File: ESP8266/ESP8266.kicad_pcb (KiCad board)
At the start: 2 copper layers, 50.8 x 25.4 mm, 52 parts, among them J1 TYPE-C, J2 Micro_SD_Card_Det_Hirose_DM3AT, J3 SirBlue, J4 Conn_01x11, J6 Conn_01x11, Q1 BSS138DW, Q2 MMBT2222A, U1 CP2104, U2 AZ1117-3.3, U3 ESP-12F

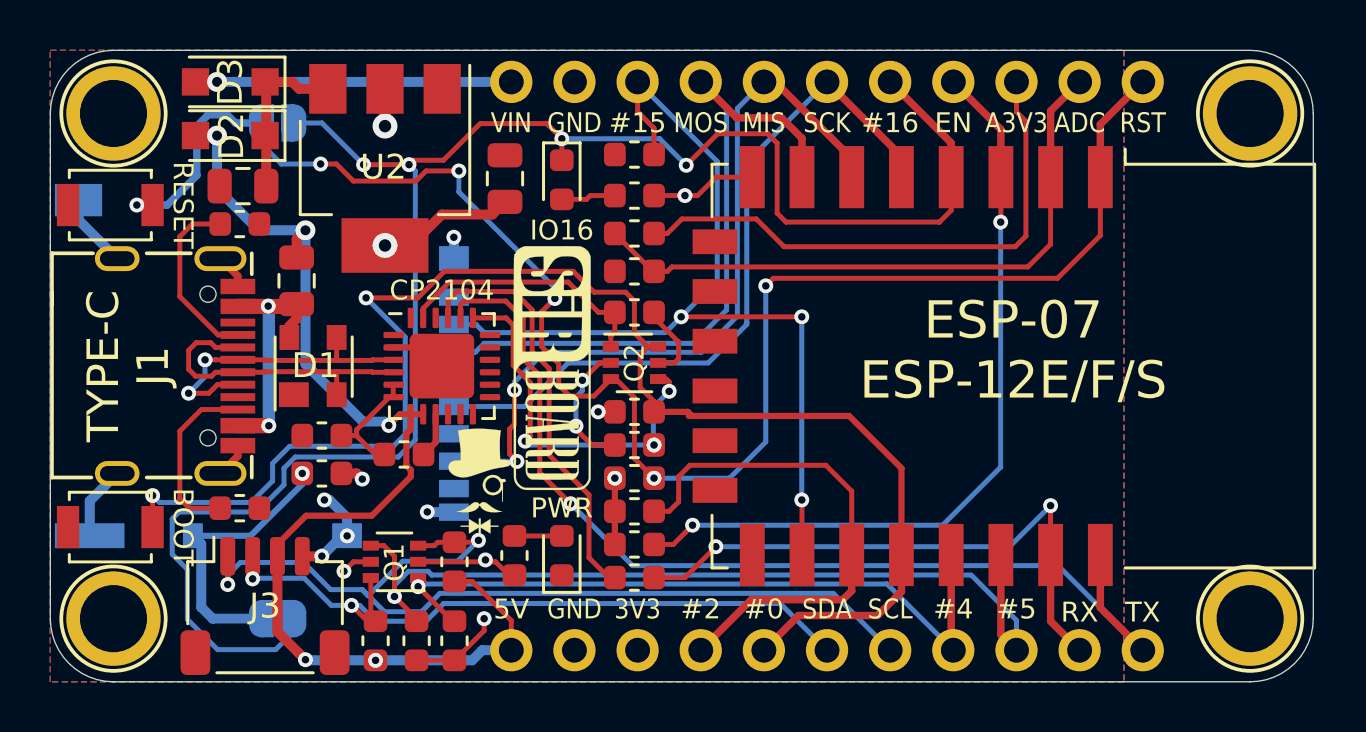
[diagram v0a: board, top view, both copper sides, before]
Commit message: ESP8266 V1.3
LED Deletes Added
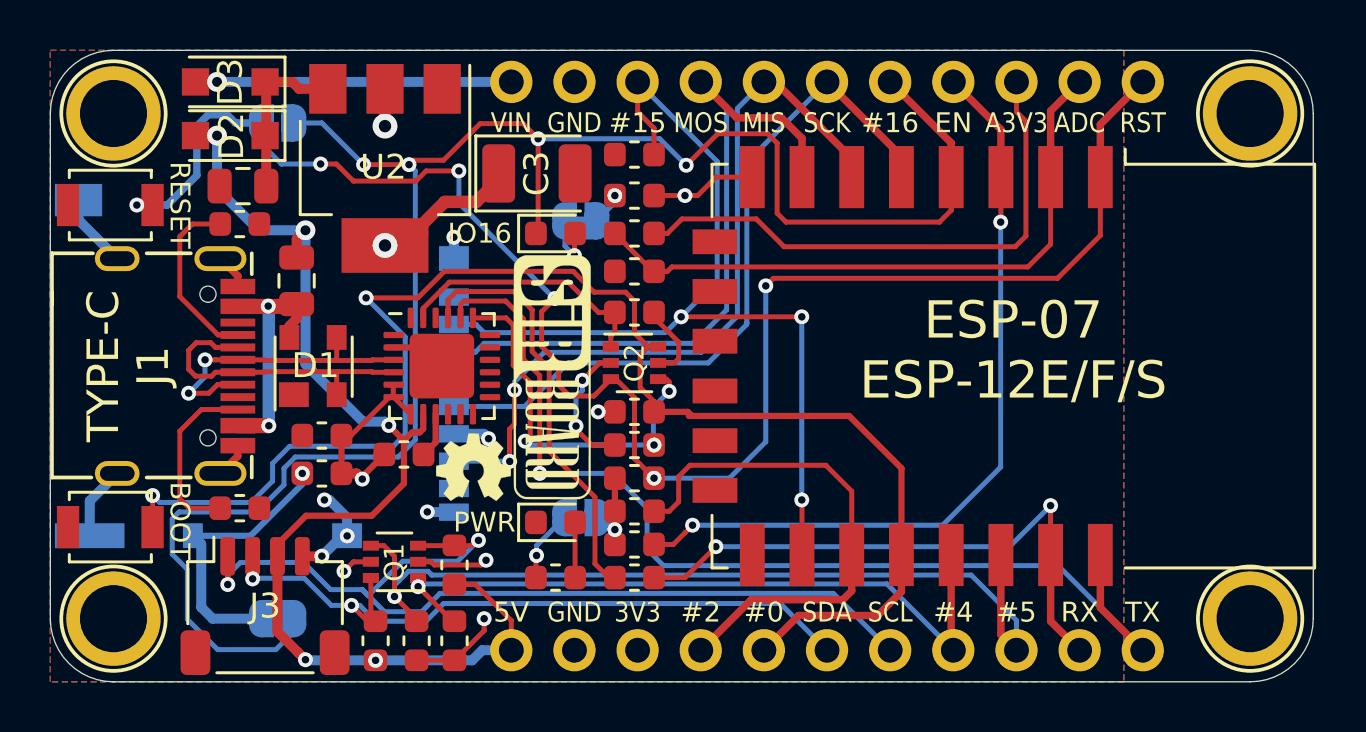
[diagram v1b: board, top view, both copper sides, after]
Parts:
- removed the G*** at (59.2, 44.0)
- added G***: LOGO, logo:OSHW44x31, F.Cu at (58.9, 43.4)
- added IO16: LED_DELETE2, SirBoardLibrary:SolderJumper-2_P1.3mm_Bridged_RoundedPad1.0x1.5mm, B.Cu at (63.2, 33.5)
- added PWR: LED_DELETE1, SirBoardLibrary:SolderJumper-2_P1.3mm_Bridged_RoundedPad1.0x1.5mm, B.Cu at (63.2, 45.5)
- C3: value 10uF -> 100uF; footprint Capacitor_SMD:C_0805_2012Metric -> Capacitor_Tantalum_SMD:CP_EIA-3528-21_Kemet-B
- HOIROSE DM3AT: renamed from J2
- moved IO16 2.17 mm to (62.2, 34.0), turned to 0 degrees
- moved R16 1.88 mm to (62.2, 47.9), turned to 0 degrees
- moved G*** 1.40 mm to (69.3, 39.4)
- moved PWR 1.36 mm to (62.2, 45.7), turned to 0 degrees
- moved C3 1.30 mm to (61.5, 31.6), turned to 0 degrees
- moved G*** 0.63 mm to (76.8, 39.4)
- moved G*** 0.37 mm to (62.1, 39.8)
- moved R7 0.13 mm to (58.2, 47.4)
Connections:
- C1 pad 1: /CP_VDD -> +3V3
- IO16 pad 2: Net-(LED2-Pad2) -> Net-(JP2-Pad2)
- R15 pad 2: Net-(LED2-Pad2) -> Net-(JP2-Pad1)
- R16 pad 1: +3V3 -> Net-(JP1-Pad2)
- R3 pad 2: /CP_VDD -> +3V3
- U1 pad 5: /CP_VDD -> +3V3
- U1 pad 6: /CP_VDD -> +3V3
- U1 pad 7: VBUS -> +3V3
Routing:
- net +3V3: track 24.8 -> 33.7 mm
- net /CP_VDD: track 4.82 -> 0.00 mm
- net GPIO16: track 71.8 -> 74.8 mm
- net Net-(JP1-Pad2): track 0.00 -> 2.89 mm, vias 0 -> 1
- net Net-(JP2-Pad2): track 0.00 -> 2.53 mm, vias 0 -> 1
- net Net-(LED2-Pad2): track 2.20 -> 0.00 mm
- net Net-(JP2-Pad1): track 0.00 -> 1.32 mm, vias 0 -> 1
- net TX_ESP: track 41.6 -> 42.6 mm
- net VBUS: track 46.8 -> 46.3 mm
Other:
- board text added: "3V3_ADC"
- board text added: "IO12"
- board text added: "IO13"
- board text added: "IO14"
- board text added: "IO15"
- board text added: "IO16 LED"
- board text added: "PWR LED"
- board text removed: "3V3 ADC"
- board text removed: "CP2104"
- board text removed: "GPIO12"
- board text removed: "GPIO13"
- board text removed: "GPIO14"
- board text removed: "GPIO15"
